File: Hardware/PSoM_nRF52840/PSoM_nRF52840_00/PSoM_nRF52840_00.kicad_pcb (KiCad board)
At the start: 6 copper layers, 26.3 x 23.2 mm, 56 parts, among them J101 DF40C-60DP-0.4V(51), J102 Bare PCB USB C, J401 Conn_01x01_Pin, J402 Conn_01x01_Pin, SW461 SW_Push, U201 NPM1300-QEAA-R, U401 nRF52840-QIAA-aQFN73, Y401 830108161301

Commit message: routing is doing great progress
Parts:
- C401, C402, Y401: moved to B.Cu
- C407: moved to F.Cu
- moved R203 19.8 mm to (154.4, 111.6)
- moved R204 19.8 mm to (154.4, 111.0)
- moved C403 6.04 mm to (133.2, 88.0)
- moved L452 6.04 mm to (132.4, 85.3)
- moved C404 6.04 mm to (133.2, 86.5)
- moved C451 6.04 mm to (133.2, 85.8)
- moved L451 6.04 mm to (131.8, 85.0)
- moved L401 6.04 mm to (133.6, 87.2)
- moved ANT450 5.31 mm to (128.3, 85.0)
- moved C402 3.50 mm to (135.9, 93.0), turned to 90 degrees
- moved C407 2.89 mm to (133.1, 99.6), turned to 45 degrees
- moved C420 2.82 mm to (134.6, 100.5), turned to 90 degrees
- moved L403 2.71 mm to (134.8, 96.4)
- moved C401 2.70 mm to (133.6, 93.0), turned to -90 degrees
- moved C421 2.70 mm to (135.7, 101.3), turned to 90 degrees
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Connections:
- U201 pad 25: unconnected-(U201-LED0-Pad25) -> /200_1S_Charger/LED0
- U201 pad 26: unconnected-(U201-LED1-Pad26) -> /200_1S_Charger/LED1
- U201 pad 27: unconnected-(U201-LED2-Pad27) -> /200_1S_Charger/LED2
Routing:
- net P31: track 0.00 -> 16.9 mm, vias 0 -> 2
- net P23: track 0.00 -> 15.1 mm, vias 0 -> 2
- net P52: track 0.00 -> 15.0 mm
- net /100_Connectors/SWDCLK: track 0.00 -> 14.4 mm
- net P29: track 0.00 -> 14.1 mm, vias 0 -> 2
- net /100_Connectors/SWDIO: track 0.00 -> 13.9 mm
- net P27: track 0.00 -> 13.1 mm, vias 0 -> 2
- net P33: track 0.00 -> 11.8 mm, vias 0 -> 2
- net P25: track 0.00 -> 11.7 mm, vias 0 -> 2
- net P46: track 0.05 -> 10.8 mm, vias 1 -> 2
- net P44: track 0.07 -> 10.3 mm, vias 1 -> 2
- net P42: track 0.00 -> 9.55 mm, vias 0 -> 2
- net P30: track 0.00 -> 8.82 mm, vias 0 -> 2
- net P32: track 0.06 -> 8.67 mm, vias 1 -> 2
- net P17: track 0.01 -> 8.43 mm, vias 1 -> 2
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
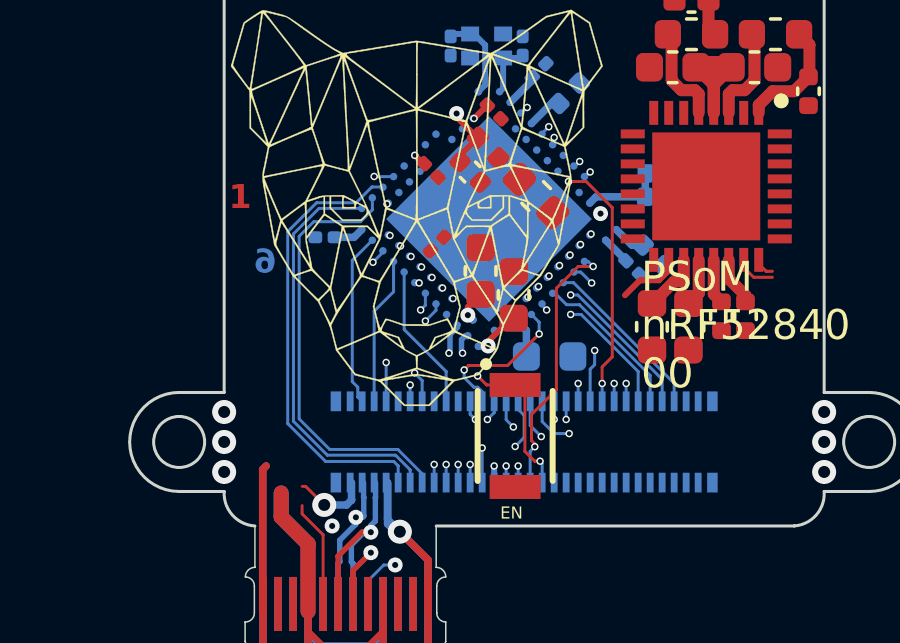
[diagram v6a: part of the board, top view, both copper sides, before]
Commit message: moved a few traces
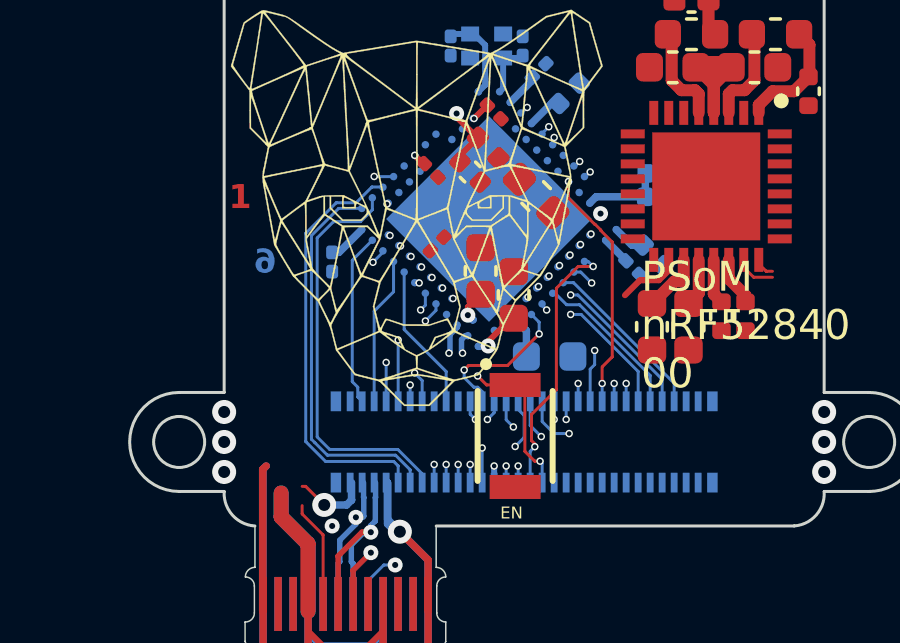
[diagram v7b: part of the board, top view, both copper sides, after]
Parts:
- moved C408 0.86 mm to (129.6, 100.2), turned to -90 degrees
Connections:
- J101 pad 51: SPI3 -> /100_Connectors/RST
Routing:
- net /100_Connectors/RST: track 9.07 -> 13.7 mm, vias 3 -> 4
- net /100_Connectors/SWDCLK: track 14.4 -> 13.6 mm
- net P52: track 15.0 -> 14.1 mm
- net /100_Connectors/SWDIO: track 13.9 -> 13.0 mm

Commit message: schematic should be done
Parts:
- added ANT450: 2450AT18A100E, Component_lib:ANTC3216X140N, F.Cu at (118.8, 119.6)
- added D201: LED, LED_SMD:LED_0402_1005Metric, F.Cu at (139.8, 84.1)
- added D202: LED, LED_SMD:LED_0402_1005Metric, F.Cu at (139.8, 86.1)
- added D203: LED, LED_SMD:LED_0402_1005Metric, F.Cu at (139.8, 88.1)
- added J1: Bare PCB USB C, Component_lib:usb-c-pcb, F.Cu at (119.6, 115.0)
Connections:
- net Net-(L402-Pad2) renamed /400-nRF52840/DCC_DEC4
- J101 pad 26: /100_Connectors/IO0 -> unconnected-(J101-Pad26)
- J101 pad 61: (no net) -> GND
- J101 pad 62: (no net) -> GND
- J101 pad 63: (no net) -> GND
- J101 pad 64: (no net) -> GND
- U401 pad D2: P13 -> /200_1S_Charger/SDA
- U401 pad F2: P15 -> /200_1S_Charger/SCL
